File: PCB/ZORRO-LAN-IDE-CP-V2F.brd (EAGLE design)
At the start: 129.5 x 79.4 mm, 77 parts, among them CN1 ZORROII_EDGE_ROUND_CONTACTS, CN2 A1200-CLOCKPORT, IC1 ENC624J600, IC2 XC95288XL-TQ144, IC3 74HCT245PW, IC4 74HCT245PW, IC5 74HCT245PW, IC7 LD117ADT33TR, IC8 AM29F010S, Q1 25MHz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

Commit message: Update in Firmware (pure Z2-AC but LAN becomes Z3) and new pcb
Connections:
- removed net LAN_CGF2: IC2.135
- net INT6: now also IC2.135
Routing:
- net INT6: track 0.00 -> 99.4 mm, vias 0 -> 2
- net A3: track 119.0 -> 115.2 mm
- net DQ14: track 106.6 -> 103.9 mm
- net DQ15: track 126.4 -> 124.3 mm
- net A4: track 121.8 -> 120.7 mm
- net A6: track 116.2 -> 115.1 mm
- net DQ7: track 168.6 -> 167.6 mm
- net DQ5: track 170.1 -> 169.2 mm
- net LEDB: track 58.7 -> 58.1 mm

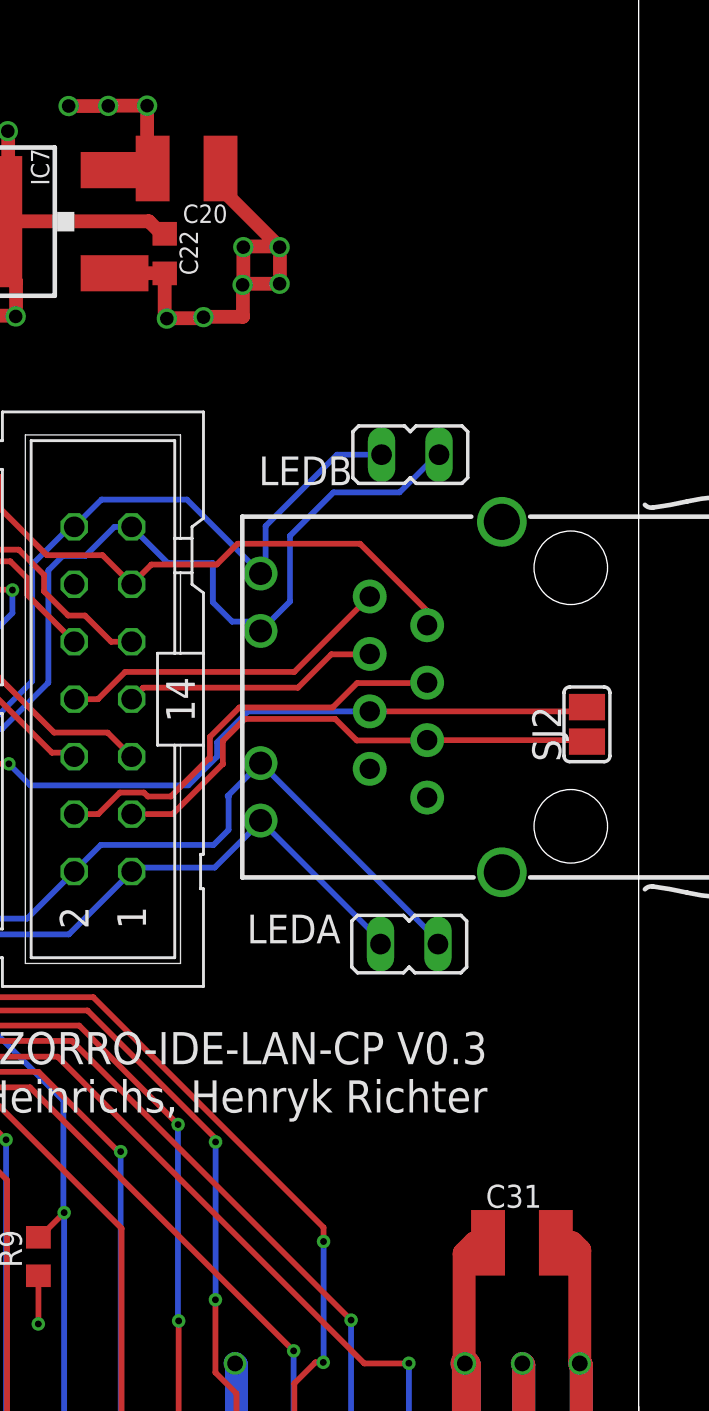
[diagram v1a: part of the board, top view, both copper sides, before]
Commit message: Firmware for new version. IDE and CP working
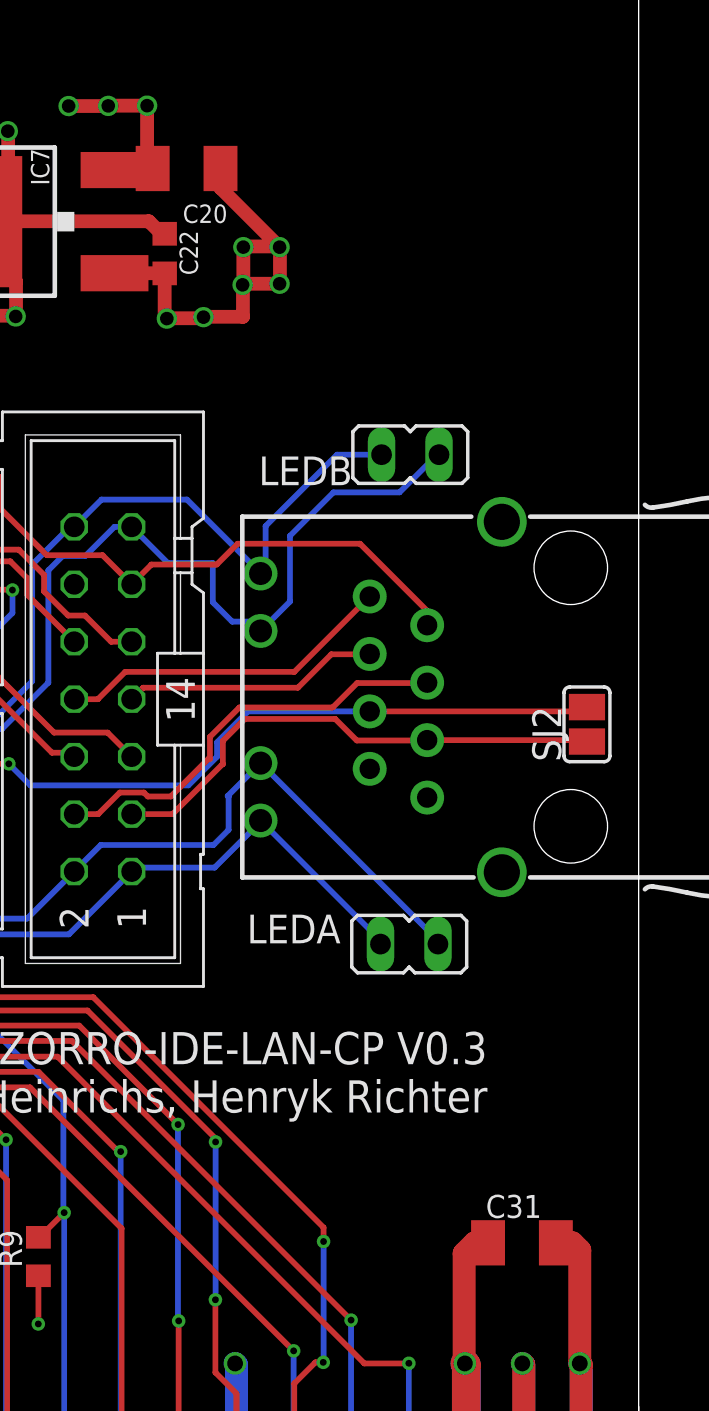
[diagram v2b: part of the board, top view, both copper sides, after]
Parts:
- C20, C31: device rcl:C1210K -> rcl:C1206K
- R12: value 3.3k -> 4.7k
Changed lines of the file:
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@@
 <?xml version="1.0" encoding="utf-8"?>
 <!DOCTYPE eagle SYSTEM "eagle.dtd">
-<eagle version="6.5.0">
+<eagle version="6.6.0">
 <drawing>
 <settings>
@@
 <attribute name="VALUE" x="44.205965625" y="67.071175" size="0.6096" layer="27" rot="R180"/>
 </element>
-<element name="C20" library="rcl" package="C1210K" value="10u" x="109.934375" y="64.5795" smashed="yes">
+<element name="C20" library="rcl" package="C1206K" value="10u" x="109.934375" y="64.5795" smashed="yes">
 <attribute name="NAME" x="109.76371875" y="62.17229375" size="0.8128" layer="25"/>
 <attribute name="VALUE" x="109.6723" y="66.20165" size="0.8128" layer="27"/>
@@
 <attribute name="VALUE" x="72.57335" y="70.147315625" size="1.016" layer="27" rot="R90"/>
 </element>
-<element name="R12" library="rcl" package="R0603" value="3.3k" x="91.028115625" y="61.5221125" smashed="yes" rot="R270">
+<element name="R12" library="rcl" package="R0603" value="4.7k" x="91.028115625" y="61.5221125" smashed="yes" rot="R270">
 <attribute name="NAME" x="91.694865625" y="63.2366125" size="1.27" layer="25" rot="R270"/>
 <attribute name="VALUE" x="89.043740625" y="63.4112375" size="1.27" layer="27" rot="R270"/>
@@
 <attribute name="VALUE" x="117.236875" y="27.3685" size="1.27" layer="27" ratio="10"/>
 </element>
-<element name="C31" library="rcl" package="C1210K" value="47u" x="124.761625" y="17.0815"/>
+<element name="C31" library="rcl" package="C1206K" value="47u" x="124.761625" y="17.0815"/>
 <element name="C32" library="rcl" package="C0603K" value="100n" x="44.54525" y="54.689375" rot="MR180"/>
 <element name="Q2" library="crystal" package="HC49UP" value="25MHz" x="82.45475" y="34.432875" smashed="yes" rot="R180">

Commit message: Improved clock startup and IDE-ROM-timing
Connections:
- net AUTO_BOOT_OFF renamed IDE_OFF
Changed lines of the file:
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@@
 <wire x1="73.457221875" y1="65.561984375" x2="73.992221875" y2="65.026984375" width="0.254" layer="1"/>
 </signal>
-<signal name="AUTO_BOOT_OFF">
+<signal name="IDE_OFF">
 <contactref element="IDE_OFF" pad="2"/>
 <contactref element="R5" pad="2"/>
